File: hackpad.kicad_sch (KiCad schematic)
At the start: 32 parts, among them J1 OLED Connection, SW1 SW_Push, SW11 RotaryEncoder_Switch, SW13 RotaryEncoder_Switch, SW2 SW_Push, SW3 SW_Push, SW4 SW_Push, SW5 SW_Push, SW6 SW_Push, SW7 SW_Push, SW8 SW_Push, U1 XIAO-RP2040-DIP

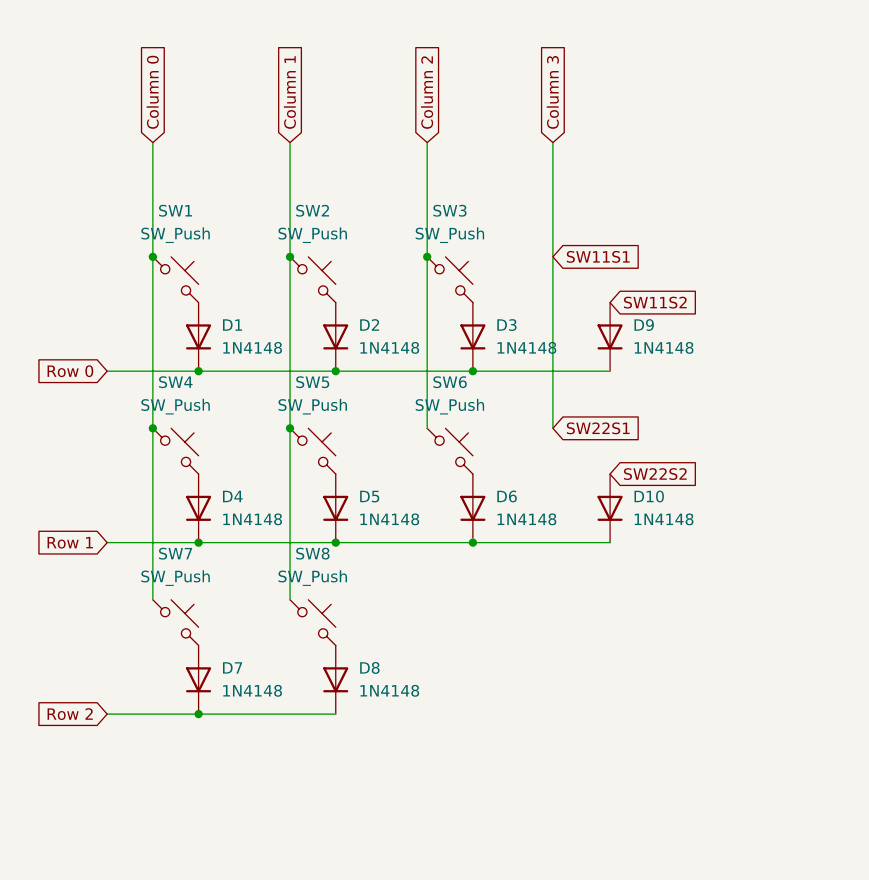
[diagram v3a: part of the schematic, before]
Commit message: finalize key and OLED screen placement
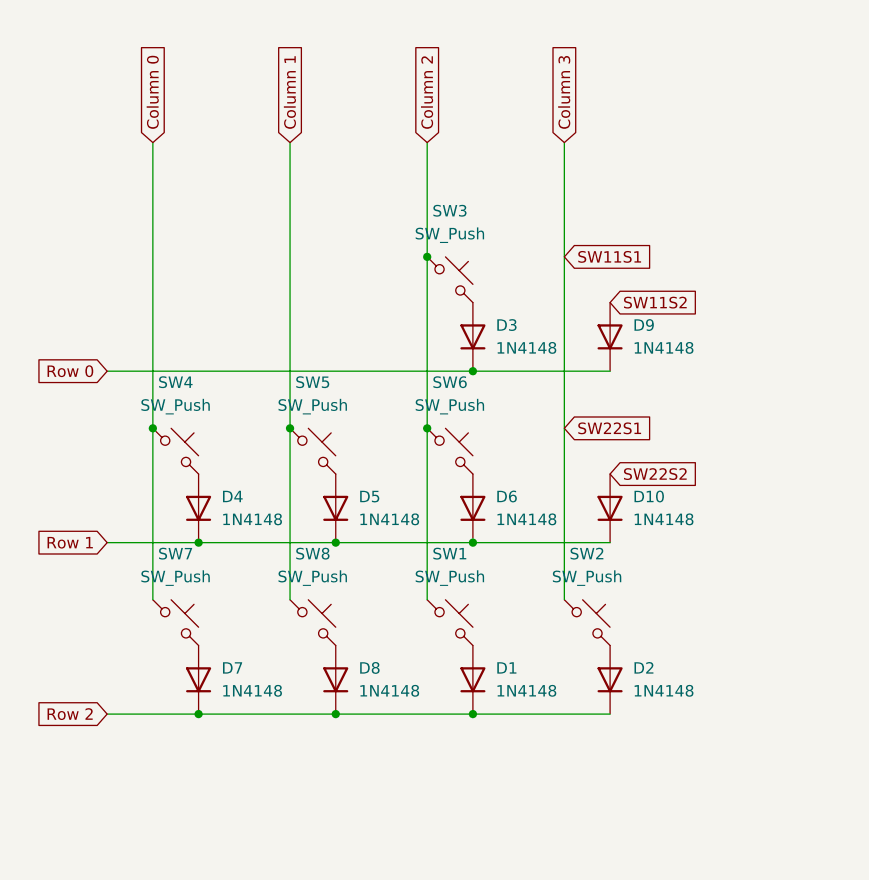
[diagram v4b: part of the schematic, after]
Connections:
- net Column 0: no longer SW1.1
- net Column 1: no longer SW2.1
- net Column 2: now also SW1.1
- net Column 3: now also SW2.1
- net Row 0: no longer D1.1 (K), D2.1 (K)
- net Row 2: now also D1.1 (K), D2.1 (K)
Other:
- moved on the sheet: D1, D2, SW1, SW2
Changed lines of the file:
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@@
 	)
 	(junction
-		(at 39.37 58.42)
+		(at 114.3 151.13)
 		(diameter 0)
 		(color 0 0 0 0)
 	)
 	(junction
-		(at 114.3 151.13)
+		(at 66.04 132.08)
 		(diameter 0)
 		(color 0 0 0 0)
 	)
 	(junction
-		(at 66.04 132.08)
+		(at 69.85 96.52)
 		(diameter 0)
 		(color 0 0 0 0)
@@
 	)
 	(junction
-		(at 90.17 132.08)
+		(at 54.61 96.52)
 		(diameter 0)
 		(color 0 0 0 0)
 	)
 	(junction
-		(at 34.29 64.77)
+		(at 90.17 132.08)
 		(diameter 0)
 		(color 0 0 0 0)
 	)
 	(junction
-		(at 54.61 58.42)
+		(at 34.29 64.77)
 		(diameter 0)
 		(color 0 0 0 0)
@@
 	)
 	(junction
-		(at 49.53 45.72)
-		(diameter 0)
-		(color 0 0 0 0)
-	)
-	(junction
 		(at 66.04 177.8)
 		(diameter 0)
@@
 	)
 	(junction
-		(at 49.53 64.77)
+		(at 64.77 64.77)
 		(diameter 0)
 		(color 0 0 0 0)
 	)
 	(junction
-		(at 34.29 45.72)
+		(at 49.53 64.77)
 		(diameter 0)
 		(color 0 0 0 0)
@@
 	(wire
 		(pts
-			(xy 49.53 45.72) (xy 49.53 64.77)
+			(xy 69.85 96.52) (xy 85.09 96.52)
+		)
+		(stroke
+			(width 0)
+			(type default)
+		)
+	)
+	(wire
+		(pts
+			(xy 49.53 33.02) (xy 49.53 64.77)
 		)
 		(stroke
@@
 	(wire
 		(pts
-			(xy 29.21 58.42) (xy 39.37 58.42)
+			(xy 29.21 58.42) (xy 69.85 58.42)
 		)
 		(stroke
@@
 	(wire
 		(pts
-			(xy 39.37 58.42) (xy 54.61 58.42)
-		)
-		(stroke
-			(width 0)
-			(type default)
-		)
-	)
-	(wire
-		(pts
 			(xy 29.21 96.52) (xy 39.37 96.52)
 		)
@@
 	(wire
 		(pts
-			(xy 218.44 90.17) (xy 218.44 86.36)
+			(xy 54.61 96.52) (xy 69.85 96.52)
 		)
 		(stroke
@@
 	(wire
 		(pts
-			(xy 176.53 52.07) (xy 166.37 52.07)
+			(xy 64.77 64.77) (xy 64.77 83.82)
+		)
+		(stroke
+			(width 0)
+			(type default)
+		)
+	)
+	(wire
+		(pts
+			(xy 218.44 90.17) (xy 218.44 86.36)
 		)
 		(stroke
@@
 	(wire
 		(pts
-			(xy 34.29 33.02) (xy 34.29 45.72)
+			(xy 176.53 52.07) (xy 166.37 52.07)
 		)
 		(stroke
@@
 	(wire
 		(pts
-			(xy 66.04 132.08) (xy 66.04 135.89)
+			(xy 80.01 33.02) (xy 80.01 83.82)
 		)
 		(stroke
@@
 	(wire
 		(pts
-			(xy 218.44 86.36) (xy 223.52 86.36)
+			(xy 66.04 132.08) (xy 66.04 135.89)
 		)
 		(stroke
@@
 	(wire
 		(pts
-			(xy 24.13 157.48) (xy 41.91 157.48)
+			(xy 218.44 86.36) (xy 223.52 86.36)
 		)
 		(stroke
@@
 	(wire
 		(pts
-			(xy 73.66 143.51) (xy 82.55 143.51)
+			(xy 24.13 157.48) (xy 41.91 157.48)
 		)
 		(stroke
@@
 	(wire
 		(pts
-			(xy 54.61 58.42) (xy 69.85 58.42)
+			(xy 73.66 143.51) (xy 82.55 143.51)
 		)
 		(stroke
@@
 	(wire
 		(pts
-			(xy 78.74 33.02) (xy 78.74 64.77)
-		)
-		(stroke
-			(width 0)
-			(type default)
-		)
-	)
-	(wire
-		(pts
 			(xy 66.04 177.8) (xy 90.17 177.8)
 		)
@@
 	(wire
 		(pts
-			(xy 49.53 33.02) (xy 49.53 45.72)
-		)
-		(stroke
-			(width 0)
-			(type default)
-		)
-	)
-	(wire
-		(pts
 			(xy 90.17 157.48) (xy 114.3 157.48)
 		)
@@
 	(wire
 		(pts
-			(xy 34.29 45.72) (xy 34.29 64.77)
+			(xy 34.29 33.02) (xy 34.29 64.77)
 		)
 		(stroke
@@
 	(global_label "SW22S1"
 		(shape input)
-		(at 78.74 64.77 0)
+		(at 80.01 64.77 0)
 		(fields_autoplaced yes)
 		(effects
@@
 		)
 		(property "Intersheetrefs" "${INTERSHEET_REFS}"
-			(at 89.2241 64.77 0)
+			(at 90.4941 64.77 0)
 			(effects
 				(font
@@
 	(global_label "SW11S1"
 		(shape input)
-		(at 78.74 45.72 0)
+		(at 80.01 45.72 0)
 		(fields_autoplaced yes)
 		(effects
@@
 		)
 		(property "Intersheetrefs" "${INTERSHEET_REFS}"
-			(at 89.2241 45.72 0)
+			(at 90.4941 45.72 0)
 			(effects
 				(font
@@
 	(global_label "Column 3"
 		(shape input)
-		(at 78.74 33.02 90)
+		(at 80.01 33.02 90)
 		(fields_autoplaced yes)
 		(effects
@@
 		)
 		(property "Intersheetrefs" "${INTERSHEET_REFS}"
-			(at 78.74 24.1082 90)
+			(at 80.01 24.1082 90)
 			(effects
 				(font
@@
 	(symbol
 		(lib_id "Switch:SW_Push_45deg")
-		(at 36.83 48.26 0)
+		(at 67.31 86.36 0)
 		(unit 1)
 		(exclude_from_sim no)
@@
 		(fields_autoplaced yes)
 		(property "Reference" "SW1"
-			(at 36.83 40.64 0)
+			(at 67.31 78.74 0)
 			(effects
 				(font
@@
 		)
 		(property "Value" "SW_Push"
-			(at 36.83 43.18 0)
+			(at 67.31 81.28 0)
 			(effects
 				(font
@@
 		)
 		(property "Footprint" "Button_Switch_Keyboard:SW_Cherry_MX_1.00u_PCB"
-			(at 36.83 48.26 0)
+			(at 67.31 86.36 0)
 			(effects
 				(font
@@
 		)
 		(property "Datasheet" "~"
-			(at 36.83 48.26 0)
+			(at 67.31 86.36 0)
 			(effects
 				(font
@@
 		)
 		(property "Description" "Push button switch, normally open, two pins, 45° tilted"
-			(at 36.83 48.26 0)
+			(at 67.31 86.36 0)
 			(effects
 				(font
@@
 	(symbol
 		(lib_id "Switch:SW_Push_45deg")
-		(at 52.07 48.26 0)
+		(at 82.55 86.36 0)
 		(unit 1)
 		(exclude_from_sim no)
@@
 		(fields_autoplaced yes)
 		(property "Reference" "SW2"
-			(at 52.07 40.64 0)
+			(at 82.55 78.74 0)
 			(effects
 				(font
@@
 		)
 		(property "Value" "SW_Push"
-			(at 52.07 43.18 0)
+			(at 82.55 81.28 0)
 			(effects
 				(font
@@
 		)
 		(property "Footprint" "Button_Switch_Keyboard:SW_Cherry_MX_1.00u_PCB"
-			(at 52.07 48.26 0)
+			(at 82.55 86.36 0)
 			(effects
 				(font
@@
 		)
 		(property "Datasheet" "~"
-			(at 52.07 48.26 0)
+			(at 82.55 86.36 0)
 			(effects
 				(font
@@
 		)
 		(property "Description" "Push button switch, normally open, two pins, 45° tilted"
-			(at 52.07 48.26 0)
+			(at 82.55 86.36 0)
 			(effects
 				(font
@@
 	(symbol
 		(lib_id "Diode:1N4148")
-		(at 54.61 54.61 90)
+		(at 85.09 92.71 90)
 		(unit 1)
 		(exclude_from_sim no)
@@
 		(fields_autoplaced yes)
 		(property "Reference" "D2"
-			(at 57.15 53.3399 90)
+			(at 87.63 91.4399 90)
 			(effects
 				(font
@@
 		)
 		(property "Value" "1N4148"
-			(at 57.15 55.8799 90)
+			(at 87.63 93.9799 90)
 			(effects
 				(font
@@
 		)
 		(property "Footprint" "Diode_THT:D_DO-35_SOD27_P7.62mm_Horizontal"
-			(at 54.61 54.61 0)
+			(at 85.09 92.71 0)
 			(effects
 				(font
@@
 		)
 		(property "Datasheet" "https://assets.nexperia.com/documents/data-sheet/1N4148_1N4448.pdf"
-			(at 54.61 54.61 0)
+			(at 85.09 92.71 0)
 			(effects
 				(font
@@
 		)
 		(property "Description" "100V 0.15A standard switching diode, DO-35"
-			(at 54.61 54.61 0)
+			(at 85.09 92.71 0)
 			(effects
 				(font
@@
 		)
 		(property "Sim.Device" "D"
-			(at 54.61 54.61 0)
+			(at 85.09 92.71 0)
 			(effects
 				(font
@@
 		)
 		(property "Sim.Pins" "1=K 2=A"
-			(at 54.61 54.61 0)
+			(at 85.09 92.71 0)
 			(effects
 				(font
@@
 	(symbol
 		(lib_id "Diode:1N4148")
-		(at 39.37 54.61 90)
+		(at 69.85 92.71 90)
 		(unit 1)
 		(exclude_from_sim no)
@@
 		(fields_autoplaced yes)
 		(property "Reference" "D1"
-			(at 41.91 53.3399 90)
+			(at 72.39 91.4399 90)
 			(effects
 				(font
@@
 		)
 		(property "Value" "1N4148"
-			(at 41.91 55.8799 90)
+			(at 72.39 93.9799 90)
 			(effects
 				(font
@@
 		)
 		(property "Footprint" "Diode_THT:D_DO-35_SOD27_P7.62mm_Horizontal"
-			(at 39.37 54.61 0)
+			(at 69.85 92.71 0)
 			(effects
 				(font
@@
 		)
 		(property "Datasheet" "https://assets.nexperia.com/documents/data-sheet/1N4148_1N4448.pdf"
-			(at 39.37 54.61 0)
+			(at 69.85 92.71 0)
 			(effects
 				(font
@@
 		)
 		(property "Description" "100V 0.15A standard switching diode, DO-35"
-			(at 39.37 54.61 0)
+			(at 69.85 92.71 0)
 			(effects
 				(font
@@
 		)
 		(property "Sim.Device" "D"
-			(at 39.37 54.61 0)
+			(at 69.85 92.71 0)
 			(effects
 				(font
@@
 		)
 		(property "Sim.Pins" "1=K 2=A"
-			(at 39.37 54.61 0)
+			(at 69.85 92.71 0)
 			(effects
 				(font

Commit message: redesign macropad
- I just realized that I forgot the row pins 〒▽〒
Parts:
- removed D4, D7: 1N4148, Diode_THT:D_DO-35_SOD27_P7.62mm_Horizontal, symbol Diode:1N4148
- removed SW13: RotaryEncoder_Switch, Rotary_Encoder:RotaryEncoder_Alps_EC11E-Switch_Vertical_H20mm, symbol Device:RotaryEncoder_Switch
- removed SW7: SW_Push, Button_Switch_Keyboard:SW_Cherry_MX_1.00u_PCB, symbol Switch:SW_Push_45deg
- renumbered D11 to LED1, D20 to LED10, D12 to LED2, D13 to LED3, D14 to LED4, D19 to LED5, D15 to LED6, D16 to LED7, D17 to LED8, D18 to LED9, SW3 to SW1, SW5 to SW2, SW6 to SW3, SW8 to SW5, SW1 to SW6, SW2 to SW7
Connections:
- net SW22A is gone; now on net Row 2: U1.9 (GPIO2/SCK)
- net SW22B is gone; now on net Row 1: U1.8 (GPIO1/RX)
- net SW22S2 is gone; now on an unnamed net: D10.2 (A)
- net Column 0: now also SW2.1, SW5.1; no longer SW4.1
- net Column 1: now also SW1.1, SW3.1, SW6.1; no longer SW2.1, SW5.1
- net Column 2: now also SW11.S1, SW4.1, SW7.1; no longer SW1.1, SW3.1, SW6.1
- net Row 0: now also U1.4 (GPIO29/ADC3/A3)
- removed net Column 3: SW11.S1, SW7.1, U1.4 (GPIO29/ADC3/A3)

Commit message: finish pcb
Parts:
- removed LED10: SK6812MINI, LED_SMD:LED_SK6812MINI_PLCC4_3.5x3.5mm_P1.75mm, symbol LED:SK6812MINI
- added D8: 1N4148, Diode_THT:D_DO-35_SOD27_P7.62mm_Horizontal, symbol Diode:1N4148
- added SW8: SW_Push, Button_Switch_Keyboard:SW_Cherry_MX_1.00u_PCB, symbol Switch:SW_Push_45deg
- XIAO-RP2040 HERE1: renamed from U1
- renumbered D3 to D1, D9 to D11, D5 to D2, D6 to D3, D10 to D4, D8 to D5, D1 to D6, D2 to D7
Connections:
- net VCC is gone; now on net +5V: J1.2 (Pin_2)
- net Column 0: now also SW8.1
- net Row 0: now also D8.1 (K)
- new net: D8.2 (A), SW8.2

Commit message: add 3D models for footprints
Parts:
- J1: footprint OLED0.91:SSD1306-0.91-OLED-4pin-128x32 -> 3D_Model_Footprints:SSD1306-0.91-OLED-4pin
- LED1, LED2, LED3, LED4, LED5, LED6, LED7, LED8, LED9: footprint LED_SMD:LED_SK6812MINI_PLCC4_3.5x3.5mm_P1.75mm -> 3D_Model_Footprints:LED_SK6812MINI_PLCC4_3.5x3.5mm_P1.75mm
- SW1, SW2, SW3, SW4, SW5, SW6, SW7, SW8: footprint Button_Switch_Keyboard:SW_Cherry_MX_1.00u_PCB -> 3D_Model_Footprints:SW_Cherry_MX_1.00u_PCB_With_3D_Model
- SW11: footprint Rotary_Encoder:RotaryEncoder_Alps_EC11E-Switch_Vertical_H20mm -> 3D_Model_Footprints:RotaryEncoder_Alps_EC11E-Switch_Vertical_H20mm
- XIAO-RP2040 HERE1: footprint OPL:XIAO-RP2040-DIP -> 3D_Model_Footprints:XIAO-RP2040-DIP
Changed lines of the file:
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@@
 			)
 		)
-		(property "Footprint" "Button_Switch_Keyboard:SW_Cherry_MX_1.00u_PCB"
+		(property "Footprint" "3D_Model_Footprints:SW_Cherry_MX_1.00u_PCB_With_3D_Model"
 			(at 67.31 86.36 0)
 			(effects
@@
 			)
 		)
-		(property "Footprint" "LED_SMD:LED_SK6812MINI_PLCC4_3.5x3.5mm_P1.75mm"
+		(property "Footprint" "3D_Model_Footprints:LED_SK6812MINI_PLCC4_3.5x3.5mm_P1.75mm"
 			(at 139.7 151.13 0)
 			(effects
@@
 			)
 		)
-		(property "Footprint" "LED_SMD:LED_SK6812MINI_PLCC4_3.5x3.5mm_P1.75mm"
+		(property "Footprint" "3D_Model_Footprints:LED_SK6812MINI_PLCC4_3.5x3.5mm_P1.75mm"
 			(at 115.57 151.13 0)
 			(effects
@@
 			)
 		)
-		(property "Footprint" "Rotary_Encoder:RotaryEncoder_Alps_EC11E-Switch_Vertical_H20mm"
+		(property "Footprint" "3D_Model_Footprints:RotaryEncoder_Alps_EC11E-Switch_Vertical_H20mm"
 			(at 143.51 48.006 0)
 			(effects
@@
 			)
 		)
-		(property "Footprint" "LED_SMD:LED_SK6812MINI_PLCC4_3.5x3.5mm_P1.75mm"
+		(property "Footprint" "3D_Model_Footprints:LED_SK6812MINI_PLCC4_3.5x3.5mm_P1.75mm"
 			(at 88.9 157.48 0)
 			(effects
@@
 			)
 		)
-		(property "Footprint" "LED_SMD:LED_SK6812MINI_PLCC4_3.5x3.5mm_P1.75mm"
+		(property "Footprint" "3D_Model_Footprints:LED_SK6812MINI_PLCC4_3.5x3.5mm_P1.75mm"
 			(at 113.03 157.48 0)
 			(effects
@@
 			)
 		)
-		(property "Footprint" "Button_Switch_Keyboard:SW_Cherry_MX_1.00u_PCB"
+		(property "Footprint" "3D_Model_Footprints:SW_Cherry_MX_1.00u_PCB_With_3D_Model"
 			(at 52.07 67.31 0)
 			(effects
@@
 			)
 		)
-		(property "Footprint" "LED_SMD:LED_SK6812MINI_PLCC4_3.5x3.5mm_P1.75mm"
+		(property "Footprint" "3D_Model_Footprints:LED_SK6812MINI_PLCC4_3.5x3.5mm_P1.75mm"
 			(at 64.77 157.48 0)
 			(effects
@@
 			)
 		)
-		(property "Footprint" "Button_Switch_Keyboard:SW_Cherry_MX_1.00u_PCB"
+		(property "Footprint" "3D_Model_Footprints:SW_Cherry_MX_1.00u_PCB_With_3D_Model"
 			(at 67.31 48.26 0)
 			(effects
@@
 			)
 		)
-		(property "Footprint" "Button_Switch_Keyboard:SW_Cherry_MX_1.00u_PCB"
+		(property "Footprint" "3D_Model_Footprints:SW_Cherry_MX_1.00u_PCB_With_3D_Model"
 			(at 82.55 67.31 0)
 			(effects
@@
 			)
 		)
-		(property "Footprint" "Button_Switch_Keyboard:SW_Cherry_MX_1.00u_PCB"
+		(property "Footprint" "3D_Model_Footprints:SW_Cherry_MX_1.00u_PCB_With_3D_Model"
 			(at 52.07 48.26 0)
 			(effects
@@
 			)
 		)
-		(property "Footprint" "LED_SMD:LED_SK6812MINI_PLCC4_3.5x3.5mm_P1.75mm"
+		(property "Footprint" "3D_Model_Footprints:LED_SK6812MINI_PLCC4_3.5x3.5mm_P1.75mm"
 			(at 43.18 151.13 0)
 			(effects
@@
 			)
 		)
-		(property "Footprint" "Button_Switch_Keyboard:SW_Cherry_MX_1.00u_PCB"
+		(property "Footprint" "3D_Model_Footprints:SW_Cherry_MX_1.00u_PCB_With_3D_Model"
 			(at 67.31 67.31 0)
 			(effects
@@
 			)
 		)
-		(property "Footprint" "LED_SMD:LED_SK6812MINI_PLCC4_3.5x3.5mm_P1.75mm"
+		(property "Footprint" "3D_Model_Footprints:LED_SK6812MINI_PLCC4_3.5x3.5mm_P1.75mm"
 			(at 91.44 151.13 0)
 			(effects
@@
 			)
 		)
-		(property "Footprint" "LED_SMD:LED_SK6812MINI_PLCC4_3.5x3.5mm_P1.75mm"
+		(property "Footprint" "3D_Model_Footprints:LED_SK6812MINI_PLCC4_3.5x3.5mm_P1.75mm"
 			(at 67.31 151.13 0)
 			(effects
@@
 			)
 		)
-		(property "Footprint" "OLED0.91:SSD1306-0.91-OLED-4pin-128x32"
+		(property "Footprint" "3D_Model_Footprints:SSD1306-0.91-OLED-4pin"
 			(at 226.06 95.25 0)
 			(effects
@@
 			)
 		)
-		(property "Footprint" "Button_Switch_Keyboard:SW_Cherry_MX_1.00u_PCB"
+		(property "Footprint" "3D_Model_Footprints:SW_Cherry_MX_1.00u_PCB_With_3D_Model"
 			(at 82.55 86.36 0)
 			(effects
@@
 			)
 		)
-		(property "Footprint" "OPL:XIAO-RP2040-DIP"
+		(property "Footprint" "3D_Model_Footprints:XIAO-RP2040-DIP"
 			(at 154.178 116.078 0)
 			(effects
@@
 			)
 		)
-		(property "Footprint" "Button_Switch_Keyboard:SW_Cherry_MX_1.00u_PCB"
+		(property "Footprint" "3D_Model_Footprints:SW_Cherry_MX_1.00u_PCB_With_3D_Model"
 			(at 52.07 86.36 0)
 			(effects
@@
 			)
 		)
-		(property "Footprint" "LED_SMD:LED_SK6812MINI_PLCC4_3.5x3.5mm_P1.75mm"
+		(property "Footprint" "3D_Model_Footprints:LED_SK6812MINI_PLCC4_3.5x3.5mm_P1.75mm"
 			(at 137.16 157.48 0)
 			(effects
